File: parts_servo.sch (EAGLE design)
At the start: 43 parts, among them Q110 PMDPB28UN, Q120 PMDPB28UN, U1 MCP1703-3302, U100 RT9625A, U20 sn65hvd72, U50 nRF51822, X60 CX3225GB16000P0HPQCC

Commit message: Initial layout
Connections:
- removed net SENSOR7: JP2.7, U50P0.00-07.P0.03
- new net SENSOR2: JP2.3, U50P0.00-07.P0.02
- net DIFFERENTIAL_INPUT: now also U50P0.24-31.P0.29; no longer U50P0.16-23.P0.21
- net DIFFERENTIAL_INPUT_EN: now also U50P0.24-31.P0.28; no longer U50P0.16-23.P0.19
- net DIFFERENTIAL_OUTPUT: now also U50P0.24-31.P0.24; no longer U50P0.16-23.P0.20
- net DIFFERENTIAL_OUTPUT_EN: now also U50P0.24-31.P0.25; no longer U50P0.16-23.P0.18
- net PWM1: now also U50P0.08-15.P0.09; no longer U50P0.08-15.P0.08
- net PWM2: now also U50P0.08-15.P0.12; no longer U50P0.08-15.P0.09
- net PWM_POR: now also U50P0.08-15.P0.08; no longer U50P0.08-15.P0.12
- net SENSOR3: now also JP2.4; no longer JP2.3
- net SENSOR4: now also JP2.5, U50P0.00-07.P0.04; no longer JP2.4, U50P0.00-07.P0.05
- net SENSOR5: now also JP2.6, U50P0.00-07.P0.03; no longer JP2.5, U50P0.00-07.P0.02
- net SENSOR6: now also JP2.7, U50P0.00-07.P0.05; no longer JP2.6, U50P0.00-07.P0.04

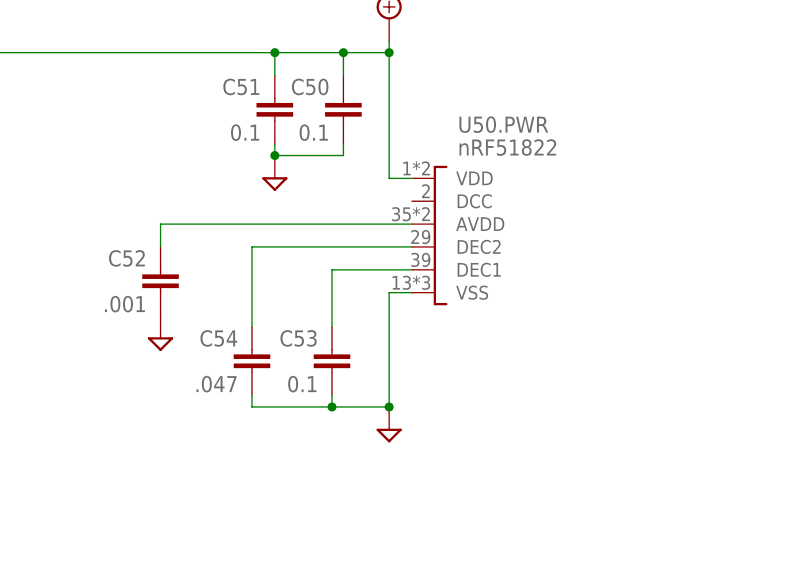
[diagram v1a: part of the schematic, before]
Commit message: Connect NRF center pad to GND.  Add ground pour on bottom of board to improve current return from motor FETs.
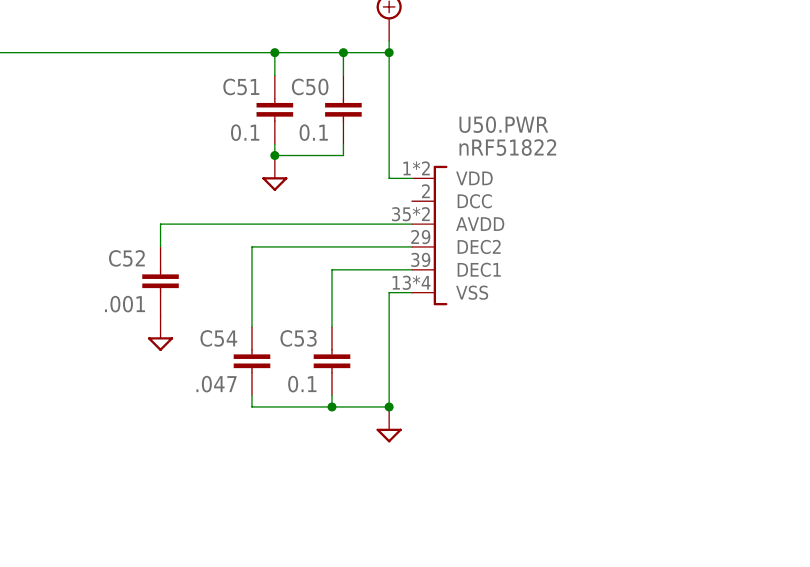
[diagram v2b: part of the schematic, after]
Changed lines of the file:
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@@
 <setting verticaltext="up"/>
 </settings>
-<grid distance="0.05" unitdist="inch" unit="inch" style="lines" multiple="1" display="yes" altdistance="0.01" altunitdist="inch" altunit="inch"/>
+<grid distance="0.1" unitdist="inch" unit="inch" style="lines" multiple="1" display="no" altdistance="0.01" altunitdist="inch" altunit="inch"/>
 <layers>
 <layer number="1" name="Top" color="4" fill="1" visible="no" active="no"/>

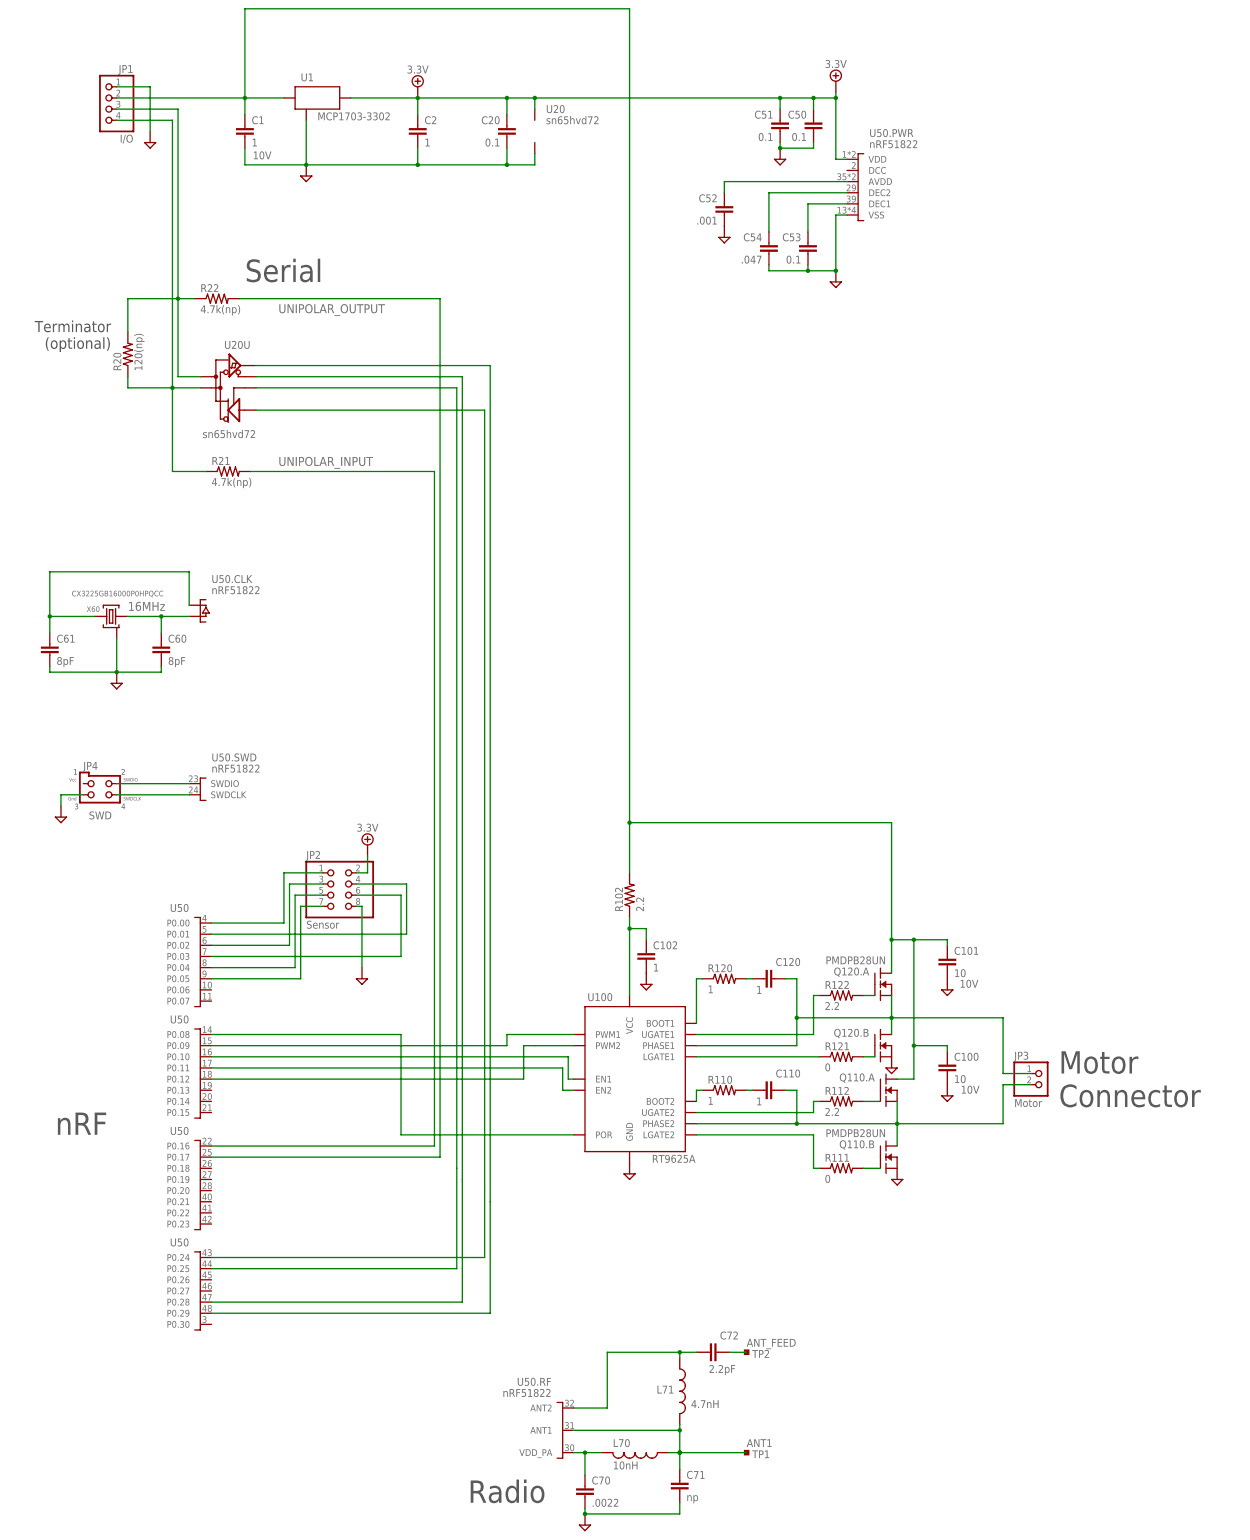
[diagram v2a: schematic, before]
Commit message: Second rev of board design.  Shrink to servo case size
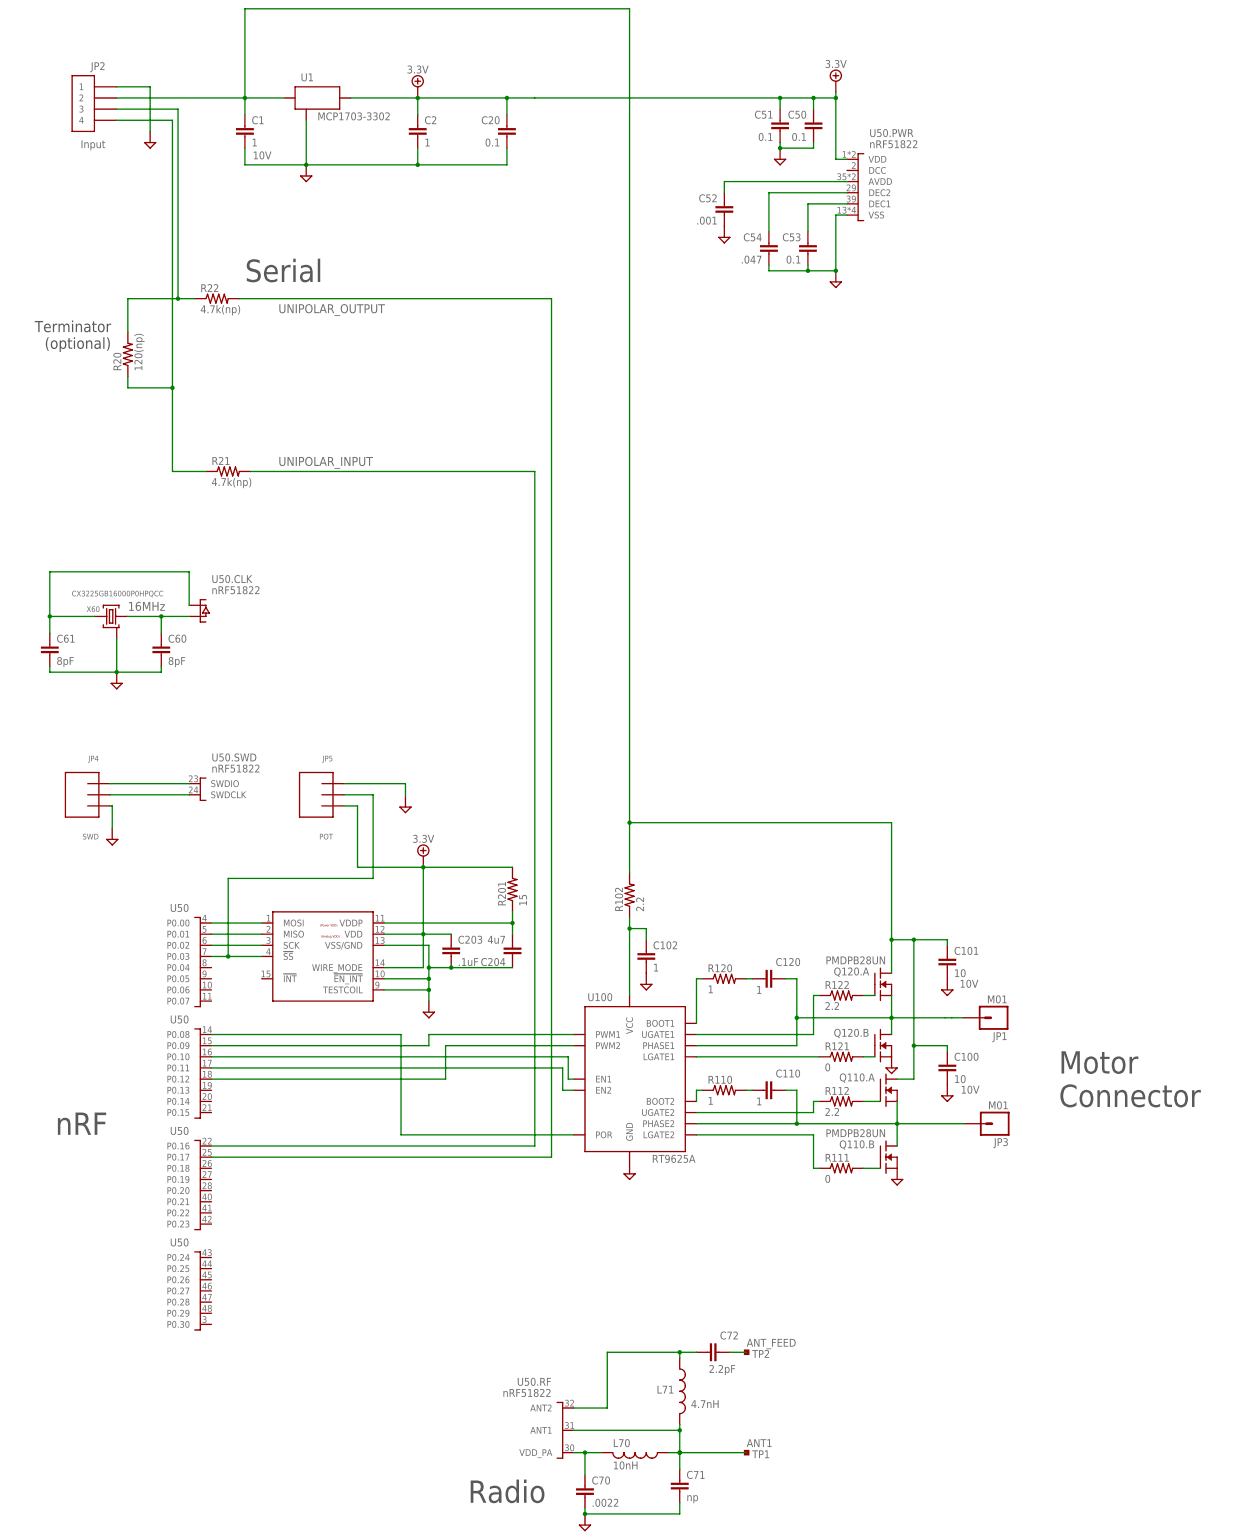
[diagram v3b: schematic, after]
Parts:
- removed U20: sn65hvd72, parts_servo:DIFFERENTIAL_TRANSCEIVER-DFN-8(3X3)+EP
- added C203: .1uF, rcl_custom:C-EU0402-B
- added C204: 4u7, rcl_custom:C-EU0402-B
- added JP5: POT, parts_servo:SMD_1X3_HEADERSMDLARGEPADS
- added R201: 15, rcl_custom:R-US_0402-B
- added U200: AS5050, parts_servo:AS5050
- JP1: value I/O -> M01; device pinhead:PINHD-1X4 -> parts_servo:M01
- JP2: value Sensor -> Input; device pinhead:PINHD-2X4 -> parts_servo:SMD_1X4_HEADER
- JP3: value Motor -> M01; device pinhead:PINHD-1X2 -> parts_servo:M01
- JP4: device parts_servo:SWD-ARM_MINI -> parts_servo:SMD_1X3_HEADER
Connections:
- removed net DIFFERENTIAL_INPUT: U20U.R, U50P0.24-31.P0.29
- removed net DIFFERENTIAL_INPUT_EN: U20U.!RE!, U50P0.24-31.P0.28
- removed net DIFFERENTIAL_OUTPUT: U20U.D, U50P0.24-31.P0.24
- removed net DIFFERENTIAL_OUTPUT_EN: U20U.DE, U50P0.24-31.P0.25
- removed net SENSOR1: JP2.1, U50P0.00-07.P0.00
- removed net SENSOR2: JP2.3, U50P0.00-07.P0.02
- removed net SENSOR3: JP2.4, U50P0.00-07.P0.01
- removed net SENSOR4: JP2.5, U50P0.00-07.P0.04
- removed net SENSOR5: JP2.6, U50P0.00-07.P0.03
- removed net SENSOR6: JP2.7, U50P0.00-07.P0.05
- new net N$1: U200.MOSI, U50P0.00-07.P0.00
- new net N$3: U200.MISO, U50P0.00-07.P0.01
- new net N$4: U200.SCK, U50P0.00-07.P0.02
- new net N$5: JP5.2, U200.!SS, U50P0.00-07.P0.03
- new net N$6: C204.2, R201.1, U200.VDDP
- net 3.3V: now also C203.1, JP5.3, R201.2, U200.VDD, U200.WIRE_MODE; no longer JP2.2, U20PWR.VDD
- net D1/TX: now also JP2.3; no longer JP1.3, U20U.A
- net D2/RX: now also JP2.4; no longer JP1.4, U20U.B
- net GND: now also C203.2, C204.1, JP2.1, JP4.3, JP5.1, U200.!EN_INT, U200.TESTCOIL, U200.VSS/GND; no longer JP1.1, JP2.8, JP4.GND, U20PWR.GND
- net MOTOR1: now also JP1.1; no longer JP3.1
- net MOTOR2: now also JP3.1; no longer JP3.2
- net POWER_IN: now also JP2.2; no longer JP1.2
- net SWDCLK: now also JP4.2; no longer JP4.SWDCLK
- net SWDIO: now also JP4.1; no longer JP4.SWDIO
